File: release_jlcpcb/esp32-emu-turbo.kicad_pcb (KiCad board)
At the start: 4 copper layers, 160 x 75 mm, 71 parts, among them J1 USB-C-16P, J3 JST-PH-2P, J4 FPC-40P-0.5mm, SW1 SW-SMD-5.1x5.1, SW10 SW-SMD-5.1x5.1, SW11 SW-SMD-5.1x5.1, SW12 SW-SMD-5.1x5.1, SW13 SW-SMD-5.1x5.1, SW2 SW-SMD-5.1x5.1, SW3 SW-SMD-5.1x5.1, SW4 SW-SMD-5.1x5.1, SW5 SW-SMD-5.1x5.1, SW6 SW-SMD-5.1x5.1, SW7 SW-SMD-5.1x5.1, SW8 SW-SMD-5.1x5.1, SW9 SW-SMD-5.1x5.1, U1 ESP32-S3-WROOM-1-N16R8, U2 ESOP-8, U3 SOT-223, U5 SOP-16, U6 TF-01A

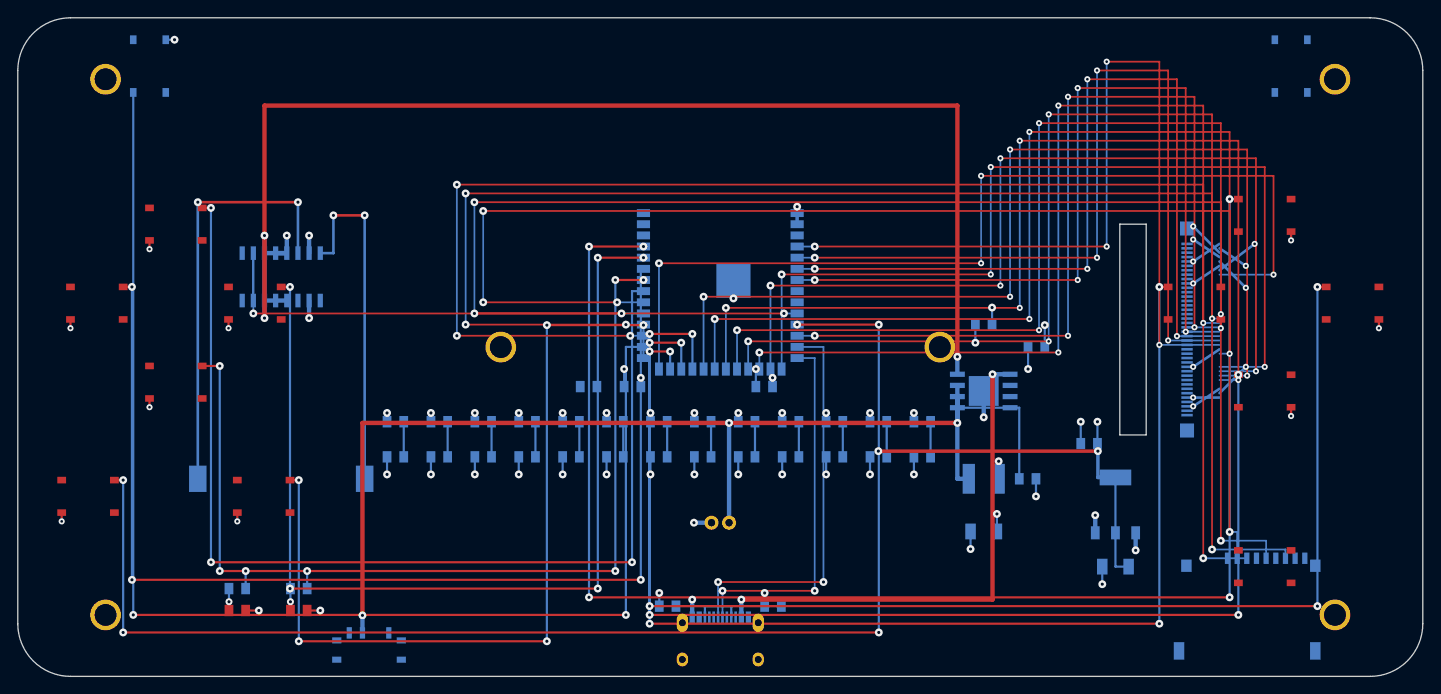
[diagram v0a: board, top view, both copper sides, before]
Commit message: Fix JLCPCB DFM issues: pad spacing, unique pad names, BTN_R routing + v2.0 release
- Reduce ESOP-8 (IP5306) exposed pad height 3.4→2.8mm for 0.2mm pad clearance
- Make MSK12C02 shell pads unique (SH→SH1-SH4) to eliminate 0mm spacing flags
- Make USB-C shield pads unique (S→S1-S4) for same reason
- Add complete BTN_R (SW12→GPIO36) routing that was missing entirely
- Add 3 regression guard tests (19-21): EP pad clearance, unique pad names, BTN_R routing
- Trace spacing violations reduced from 27 to 17 baseline
- All 27/27 DFM tests pass
- Generate JLCPCB v2.0 release files (gerbers, CPL, BOM)

Co-Authored-By: Claude Opus 4.6 <noreply@anthropic.com>
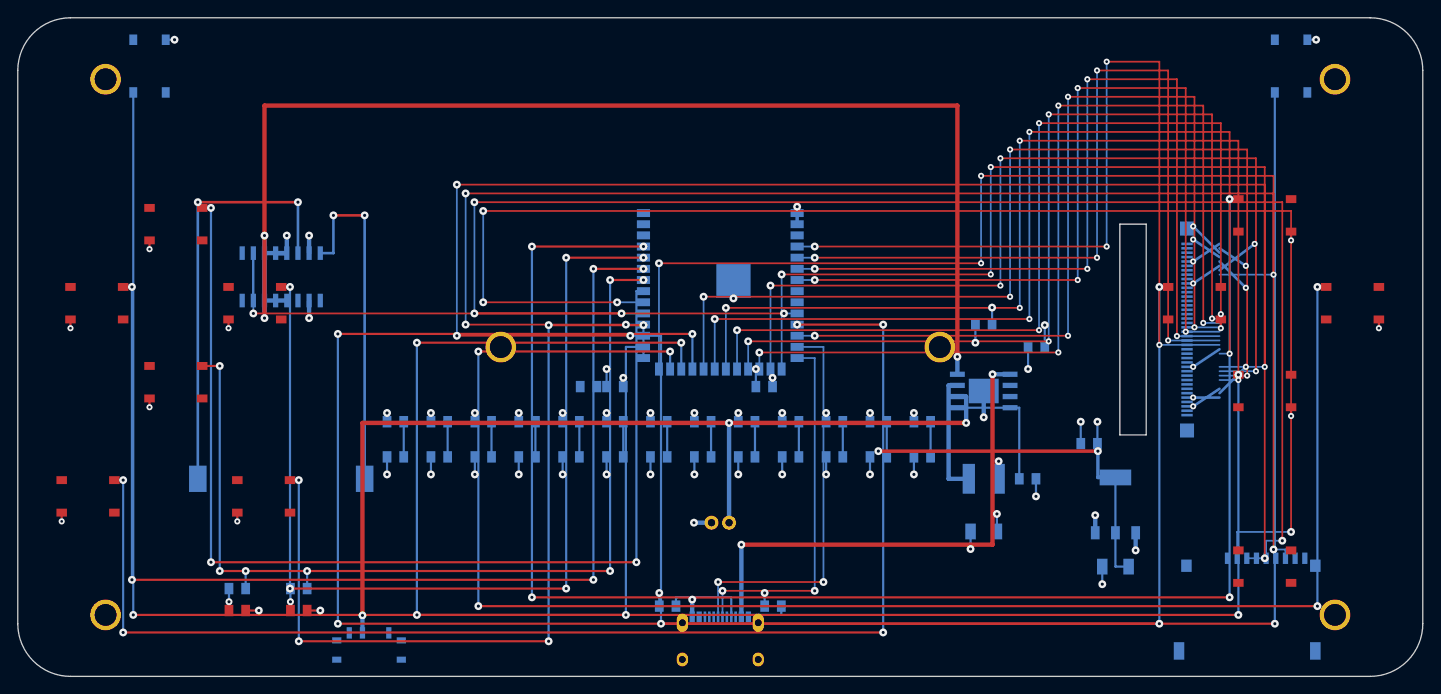
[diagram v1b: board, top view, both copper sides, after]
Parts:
- moved C3 2.00 mm to (68.0, 42.0)
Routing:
- net BTN_R: track 4.00 -> 169.2 mm, vias 0 -> 2
- net BTN_Y: track 143.3 -> 214.3 mm
- net BTN_X: track 136.0 -> 189.0 mm
- net BTN_B: track 150.7 -> 189.7 mm
- net BTN_A: track 169.5 -> 182.5 mm
- net SD_CS: track 154.1 -> 166.3 mm
- net SD_MOSI: track 171.0 -> 175.1 mm
- net SD_CLK: track 162.6 -> 166.3 mm
- net USB_CC1: track 7.55 -> 9.55 mm
- net LX: track 11.9 -> 13.9 mm
- net BAT+: track 110.5 -> 112.5 mm
- net GND: track 101.7 -> 102.7 mm, vias 50 -> 51
- net BTN_START: track 152.8 -> 153.8 mm
- net BTN_LEFT: vias 3 -> 5

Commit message: Fix 5 KiCad DRC clearance violations + add 2 regression guards (33 DFM tests)
SD routing post_slot_map redesigned to avoid conflicts:
- Replaced x=143,144 with x=137,140 to clear SW5/SW7 GND vias at x=143.5
  (was 0.05mm gap, required 0.2mm; now 3.5mm+ clearance)
- bypass_y shifted from 19-22 to 17-20 to clear SW5[2] pad at y=20.65
  (via at (146,20) had -0.003mm edge overlap; now 2.24mm clearance at y=18)
- x=150 replaced with x=140 after mounting hole at (150,68) co-located with
  SD_CLK stagger_y=68 via; x=140 gives 10mm clearance from hole
- All 6 via-to-via pairwise gaps now >= 2mm (min 1.15mm required)

BAT+ via at L1[1] offset 0.7mm right to x=112.4:
- Was (111.7, 49.5): exactly touching VBUS F.Cu trace at x=111.0 (gap=0.0mm)
- Now (112.4, 49.5): gap to VBUS right edge = 0.70mm (cleared)

LED GND via offset reduced from 1.5mm to 1.0mm:
- Was (34.45, 67.5): 0.175mm from BTN_SELECT B.Cu trace at x=35.2
- Now (33.95, 67.5): gap = 0.675mm (cleared)

New regression tests: test_sd_gnd_via_clearance (Test 25) guards SD B.Cu
verticals from x=[142.75,144.25] zone; test_bat_plus_via_vbus_clearance
(Test 26) guards L1 BAT+ via against VBUS trace. All 33 DFM tests pass.

Co-Authored-By: Claude Opus 4.6 <noreply@anthropic.com>
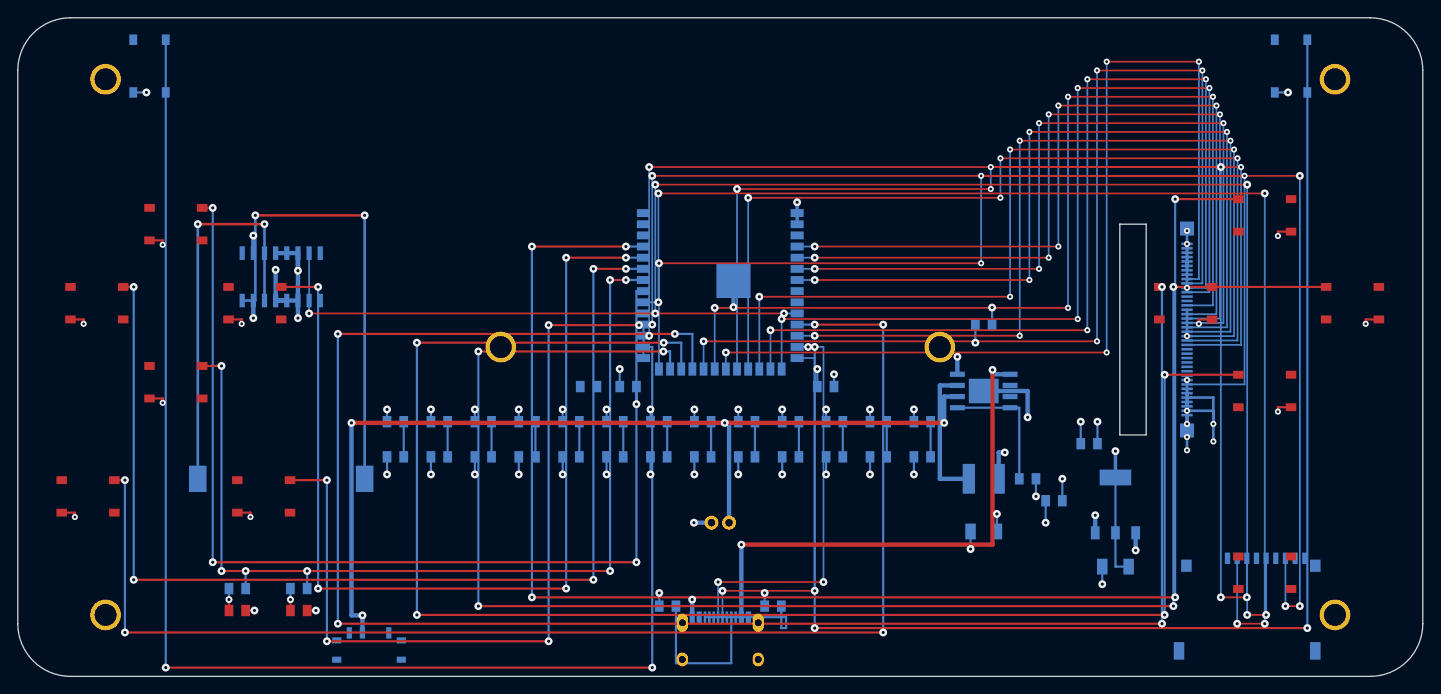
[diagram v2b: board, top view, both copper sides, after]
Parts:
- moved C18 17.6 mm to (118.0, 55.0)
- moved C4 7.00 mm to (92.0, 42.0)
- moved C3 1.50 mm to (69.5, 42.0)
- moved SW8 1.00 mm to (133.0, 32.5)
- moved SW13 0.70 mm to (142.0, 63.2)
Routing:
- net +5V: track 157.9 -> 27.8 mm
- net SD_MOSI: track 175.1 -> 141.4 mm, vias 4 -> 5
- net SD_CLK: track 166.3 -> 141.0 mm, vias 4 -> 5
- net SD_CS: track 166.3 -> 142.7 mm, vias 4 -> 5
- net SD_MISO: track 170.1 -> 147.8 mm, vias 4 -> 5
- net +3V3: track 78.3 -> 59.2 mm, vias 24 -> 23
- net BTN_L: track 152.1 -> 168.4 mm
- net GND: track 102.7 -> 118.0 mm
- net SPK+: track 39.4 -> 53.6 mm
- net I2S_DOUT: track 74.2 -> 62.4 mm
- net LCD_D0: track 101.4 -> 90.9 mm
- net LCD_BL: track 109.4 -> 119.0 mm
- net LCD_D1: track 100.2 -> 91.5 mm
- net USB_CC1: track 9.55 -> 18.1 mm
- net BTN_R: track 169.2 -> 161.1 mm, vias 2 -> 4
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
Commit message: Update release_jlcpcb with v2.2 gerbers, BOM and CPL
Co-Authored-By: Claude Opus 4.6 <noreply@anthropic.com>
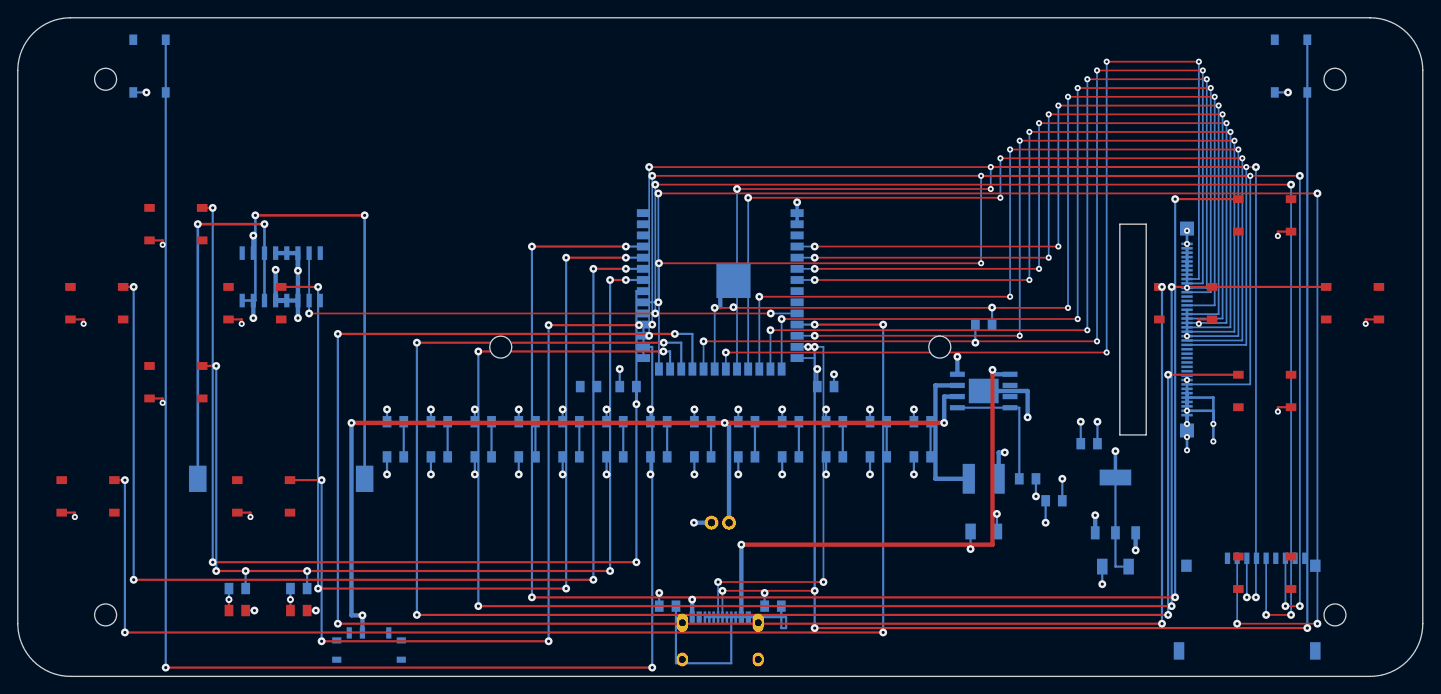
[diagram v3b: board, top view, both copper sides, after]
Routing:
- net SD_CS: track 142.7 -> 154.7 mm
- net SD_CLK: track 141.0 -> 146.7 mm
- net SD_MOSI: track 141.4 -> 143.4 mm
- net GND: track 118.0 -> 119.5 mm
- net LCD_BL: track 119.0 -> 120.3 mm
- net LCD_D7: track 106.8 -> 108.0 mm
- net LCD_D6: track 106.2 -> 107.3 mm
- net LX: track 15.9 -> 16.9 mm
- net LCD_D5: track 105.7 -> 106.7 mm
- net LCD_D4: track 98.3 -> 99.2 mm
- net LCD_D3: track 92.6 -> 93.4 mm
- net LCD_D2: track 92.0 -> 92.7 mm
- net LCD_D1: track 91.5 -> 92.1 mm
- net LCD_D0: track 90.9 -> 91.4 mm
